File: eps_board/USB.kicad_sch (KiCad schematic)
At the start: 4 parts, among them J12 10155435-00011LF

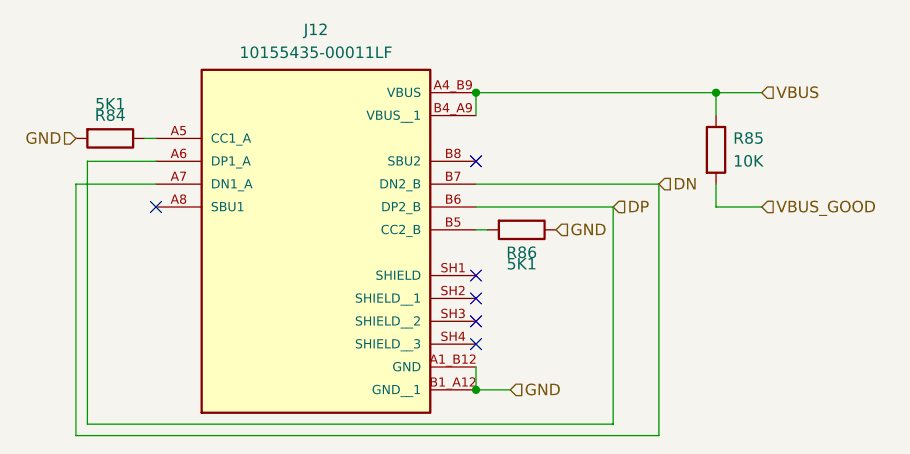
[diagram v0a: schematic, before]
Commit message: cleaning up bom: remove main camera port since it has not pullups and capacitors, correcting some errors in camera switch
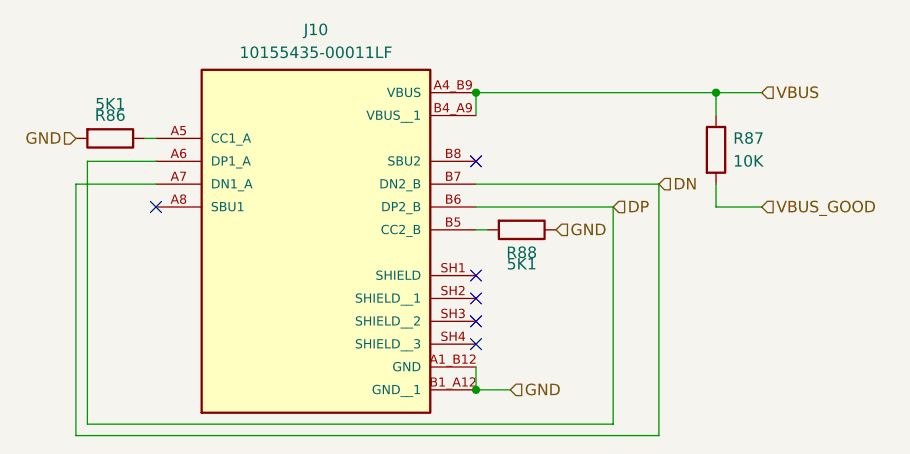
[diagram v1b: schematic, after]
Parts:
- renumbered J12 to J10, R84 to R86, R85 to R87, R86 to R88
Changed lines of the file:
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@@
 		(dnp no)
 		(fields_autoplaced yes)
-		(property "Reference" "R85"
+		(property "Reference" "R87"
 			(at 189.865 83.1849 0)
 			(effects
@@
 		)
 		(property "Tolerance" "1"
+			(at 187.96 84.455 0)
+			(effects
+				(font
+					(size 1.27 1.27)
+				)
+				(hide yes)
+			)
+		)
+		(property "MANUFACTURER" ""
+			(at 187.96 84.455 0)
+			(effects
+				(font
+					(size 1.27 1.27)
+				)
+				(hide yes)
+			)
+		)
+		(property "MAXIMUM_PACKAGE_HEIGHT" ""
+			(at 187.96 84.455 0)
+			(effects
+				(font
+					(size 1.27 1.27)
+				)
+				(hide yes)
+			)
+		)
+		(property "Manufactorer" ""
+			(at 187.96 84.455 0)
+			(effects
+				(font
+					(size 1.27 1.27)
+				)
+				(hide yes)
+			)
+		)
+		(property "PARTREV" ""
+			(at 187.96 84.455 0)
+			(effects
+				(font
+					(size 1.27 1.27)
+				)
+				(hide yes)
+			)
+		)
+		(property "STANDARD" ""
 			(at 187.96 84.455 0)
 			(effects
@@
 			(project "EPS"
 				(path "/05170af6-30ef-4c3a-b972-f098085da1bc/dffa178b-07a8-4735-b10c-32a6042c7f6e"
-					(reference "R85")
+					(reference "R87")
 					(unit 1)
 				)
@@
 		(dnp no)
 		(fields_autoplaced yes)
-		(property "Reference" "J12"
+		(property "Reference" "J10"
 			(at 143.51 71.12 0)
 			(effects
@@
 		)
 		(property "Manufacturer" "Amphenol"
+			(at 143.51 88.265 0)
+			(effects
+				(font
+					(size 1.27 1.27)
+				)
+				(hide yes)
+			)
+		)
+		(property "MANUFACTURER" ""
+			(at 143.51 88.265 0)
+			(effects
+				(font
+					(size 1.27 1.27)
+				)
+				(hide yes)
+			)
+		)
+		(property "MAXIMUM_PACKAGE_HEIGHT" ""
+			(at 143.51 88.265 0)
+			(effects
+				(font
+					(size 1.27 1.27)
+				)
+				(hide yes)
+			)
+		)
+		(property "Manufactorer" ""
+			(at 143.51 88.265 0)
+			(effects
+				(font
+					(size 1.27 1.27)
+				)
+				(hide yes)
+			)
+		)
+		(property "PARTREV" ""
+			(at 143.51 88.265 0)
+			(effects
+				(font
+					(size 1.27 1.27)
+				)
+				(hide yes)
+			)
+		)
+		(property "STANDARD" ""
 			(at 143.51 88.265 0)
 			(effects
@@
 			(project "EPS"
 				(path "/05170af6-30ef-4c3a-b972-f098085da1bc/dffa178b-07a8-4735-b10c-32a6042c7f6e"
-					(reference "J12")
+					(reference "J10")
 					(unit 1)
 				)
@@
 		(on_board yes)
 		(dnp no)
-		(property "Reference" "R86"
+		(property "Reference" "R88"
 			(at 166.37 95.885 90)
 			(effects
@@
 		)
 		(property "Manufacturer" "YAGEO"
+			(at 166.37 93.345 0)
+			(effects
+				(font
+					(size 1.27 1.27)
+				)
+				(hide yes)
+			)
+		)
+		(property "MANUFACTURER" ""
+			(at 166.37 93.345 0)
+			(effects
+				(font
+					(size 1.27 1.27)
+				)
+				(hide yes)
+			)
+		)
+		(property "MAXIMUM_PACKAGE_HEIGHT" ""
+			(at 166.37 93.345 0)
+			(effects
+				(font
+					(size 1.27 1.27)
+				)
+				(hide yes)
+			)
+		)
+		(property "Manufactorer" ""
+			(at 166.37 93.345 0)
+			(effects
+				(font
+					(size 1.27 1.27)
+				)
+				(hide yes)
+			)
+		)
+		(property "PARTREV" ""
+			(at 166.37 93.345 0)
+			(effects
+				(font
+					(size 1.27 1.27)
+				)
+				(hide yes)
+			)
+		)
+		(property "STANDARD" ""
 			(at 166.37 93.345 0)
 			(effects
@@
 			(project "EPS"
 				(path "/05170af6-30ef-4c3a-b972-f098085da1bc/dffa178b-07a8-4735-b10c-32a6042c7f6e"
-					(reference "R86")
+					(reference "R88")
 					(unit 1)
 				)
@@
 		(on_board yes)
 		(dnp no)
-		(property "Reference" "R84"
+		(property "Reference" "R86"
 			(at 120.65 80.645 90)
 			(effects
@@
 		)
 		(property "Manufacturer" "YAGEO"
+			(at 120.65 83.185 0)
+			(effects
+				(font
+					(size 1.27 1.27)
+				)
+				(hide yes)
+			)
+		)
+		(property "MANUFACTURER" ""
+			(at 120.65 83.185 0)
+			(effects
+				(font
+					(size 1.27 1.27)
+				)
+				(hide yes)
+			)
+		)
+		(property "MAXIMUM_PACKAGE_HEIGHT" ""
+			(at 120.65 83.185 0)
+			(effects
+				(font
+					(size 1.27 1.27)
+				)
+				(hide yes)
+			)
+		)
+		(property "Manufactorer" ""
+			(at 120.65 83.185 0)
+			(effects
+				(font
+					(size 1.27 1.27)
+				)
+				(hide yes)
+			)
+		)
+		(property "PARTREV" ""
+			(at 120.65 83.185 0)
+			(effects
+				(font
+					(size 1.27 1.27)
+				)
+				(hide yes)
+			)
+		)
+		(property "STANDARD" ""
 			(at 120.65 83.185 0)
 			(effects
@@
 			(project "EPS"
 				(path "/05170af6-30ef-4c3a-b972-f098085da1bc/dffa178b-07a8-4735-b10c-32a6042c7f6e"
-					(reference "R84")
+					(reference "R86")
 					(unit 1)
 				)
